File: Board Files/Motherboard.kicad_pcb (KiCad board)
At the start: 2 copper layers, 0 parts

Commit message: + Started board outline + Finished up the schematic (hopefully) + Started creation of custom footprints
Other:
- board outline added: 106 x 155 mm
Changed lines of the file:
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@@
   (general
     (thickness 1.6)
-    (drawings 0)
+    (drawings 5)
     (tracks 0)
     (zones 0)
@@
     (nets 1)
   )
-  (page A4)
+  (page A)
   (layers
     (0 F.Cu signal)
@@
     (uvia_drill 0.1)
   )
+  (gr_line (start 132.87 184.79) (end 34.15 184.79) (layer Edge.Cuts) (width 0.05))
+  (gr_line (start 140.2 177.76) (end 140.2 29.79) (layer Edge.Cuts) (width 0.05))
+  (gr_line (start 140.2 177.76) (end 132.87 184.79) (layer Edge.Cuts) (width 0.05))
+  (gr_line (start 34.15 29.79) (end 140.2 29.79) (layer Edge.Cuts) (width 0.05))
+  (gr_line (start 34.15 29.79) (end 34.15 184.79) (layer Edge.Cuts) (width 0.05))
 )

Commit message: + Completed schematic + Added RF Modulator schematic symbol + Added RF Modulator footprint + Added Reset Switch footprint + Completed Power Switch footprint + Continued board layout
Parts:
- added ACPLUG1: , Connector_BarrelJack:BarrelJack_CUI_PJ-102AH_Horizontal, F.Cu at (48.4, 6.95)
- added BC1: 10nF, Capacitor_THT:C_Disc_D6.0mm_W2.5mm_P5.00mm, F.Cu at (-118.4, -29.9)
- added C1: 100uF, Capacitor_THT:CP_Radial_D5.0mm_P2.50mm, F.Cu at (-85.6, -45.9)
- added C10: 10nF, Capacitor_THT:C_Disc_D3.0mm_W1.6mm_P2.50mm, F.Cu at (-125.3, -30.3)
- added C11: 0.47uF, Capacitor_THT:CP_Radial_D5.0mm_P2.50mm, F.Cu at (-85.6, -39.3)
- added C12: 10nF, Capacitor_THT:C_Disc_D3.0mm_W1.6mm_P2.50mm, F.Cu at (-118.4, -26.3)
- added C13: 1500uF, Capacitor_THT:CP_Radial_D12.5mm_P5.00mm, F.Cu at (87.5, -10.7)
- added C14: 1uF, Capacitor_THT:CP_Radial_D5.0mm_P2.50mm, F.Cu at (-79.0, -45.9)
- added C14: 1uF, Capacitor_THT:CP_Radial_D5.0mm_P2.50mm, F.Cu at (81.6, -15.8)
- added C15: 330pF, Capacitor_THT:C_Disc_D3.0mm_W1.6mm_P2.50mm, F.Cu at (-109.4, -18.2)
- added C16: 330pF, Capacitor_THT:C_Disc_D3.0mm_W1.6mm_P2.50mm, F.Cu at (-90.8, -34.5)
- added C17: 330pF, Capacitor_THT:C_Disc_D3.0mm_W1.6mm_P2.50mm, F.Cu at (-95.5, -29.9)
- added C19: 330pF, Capacitor_THT:C_Disc_D3.0mm_W1.6mm_P2.50mm, F.Cu at (-79.5, -41.0)
- added C2: 330pF, Capacitor_THT:C_Disc_D3.0mm_W2.0mm_P2.50mm, F.Cu at (-89.8, -31.1)
- added C20: 330pF, Capacitor_THT:C_Disc_D3.0mm_W1.6mm_P2.50mm, F.Cu at (-95.5, -26.7)
- added C21: 330pF, Capacitor_THT:C_Disc_D3.0mm_W1.6mm_P2.50mm, F.Cu at (-103.7, -19.8)
- added C22: 330pF, Capacitor_THT:C_Disc_D3.0mm_W1.6mm_P2.50mm, F.Cu at (-98.8, -23.3)
- added C23: 330pF, Capacitor_THT:C_Disc_D3.0mm_W1.6mm_P2.50mm, F.Cu at (-85.2, -34.5)
- added C24: 10nF, Capacitor_THT:C_Disc_D5.0mm_W2.5mm_P5.00mm, F.Cu at (-94.3, -47.2)
- added C25: 330pF, Capacitor_THT:C_Disc_D3.0mm_W1.6mm_P2.50mm, F.Cu at (-79.5, -37.9)
- added C26: 330pF, Capacitor_THT:C_Disc_D3.0mm_W1.6mm_P2.50mm, F.Cu at (-89.8, -27.8)
- added C27: 10nF, Capacitor_THT:C_Disc_D5.0mm_W2.5mm_P5.00mm, F.Cu at (-99.0, -37.5)
- added C28: 10nF, Capacitor_THT:C_Disc_D6.0mm_W2.5mm_P5.00mm, F.Cu at (-99.0, -33.5)
- added C3: 1uF, Capacitor_THT:CP_Radial_D5.0mm_P2.50mm, F.Cu at (-101.6, -28.2)
- added C30: 10nF, Capacitor_THT:C_Disc_D5.0mm_W2.5mm_P5.00mm, F.Cu at (-112.6, -25.8)
- added C31: 10nF, Capacitor_THT:C_Disc_D5.0mm_W2.5mm_P5.00mm, F.Cu at (-91.8, -51.6)
- added C36: 10nF, Capacitor_THT:C_Disc_D5.0mm_W2.5mm_P5.00mm, F.Cu at (-112.6, -21.8)
- added C37: 10nF, Capacitor_THT:C_Disc_D5.0mm_W2.5mm_P5.00mm, F.Cu at (-94.3, -43.2)
- added C38: 10nF, Capacitor_THT:C_Disc_D5.0mm_W2.5mm_P5.00mm, F.Cu at (-83.7, -51.2)
- added C46: 100nF, Capacitor_THT:C_Disc_D7.0mm_W2.5mm_P5.00mm, F.Cu at (-131.5, -17.9)
- added C5: 10nF, Capacitor_THT:C_Disc_D5.0mm_W2.5mm_P5.00mm, F.Cu at (-110.3, -30.7)
- added C6: 10nF, Capacitor_THT:C_Disc_D5.0mm_W2.5mm_P5.00mm, F.Cu at (-123.2, -17.9)
- added C7: 330pF, Capacitor_THT:C_Disc_D3.0mm_W1.6mm_P2.50mm, F.Cu at (-98.1, -20.2)
- added C8: 10nF, Capacitor_THT:C_Disc_D3.0mm_W2.0mm_P2.50mm, F.Cu at (-115.0, -18.0)
- added C9: 10pF, Capacitor_THT:C_Disc_D3.0mm_W2.0mm_P2.50mm, F.Cu at (-104.5, -23.1)
- added DA1: DAN601, Resistor_THT:R_Array_SIP7, F.Cu at (34.7, -127.1)
- added DA2: UPA64H, Resistor_THT:R_Array_SIP7, F.Cu at (34.7, -124.5)
- added DA3: DAN601, Resistor_THT:R_Array_SIP7, F.Cu at (14.5, -127.1)
- added DA4: UPA64H, Resistor_THT:R_Array_SIP7, F.Cu at (14.5, -124.5)
- added DB1: RC203, Diode_THT:Diode_Bridge_Round_D9.0mm, F.Cu at (75.8, -15.2)
- added FC1: 39u, Resistor_THT:R_Axial_DIN0207_L6.3mm_D2.5mm_P10.16mm_Horizontal, F.Cu at (-112.3, -34.8)
- added FC2: Ferrite_Coil, Resistor_THT:R_Axial_DIN0207_L6.3mm_D2.5mm_P10.16mm_Horizontal, F.Cu at (-145.0, -26.7)
- added P1: 72-Pin Connector, Toploader:Cart Connector, F.Cu at (9.25, -32.2)
- added P2: PowerSw, Toploader:PowerSwitch, F.Cu at (96.8, -122.5)
- added P3: ResetSw, Toploader:ResetSwitch, F.Cu at (75.6, -127.3)
- added P4: Controller_Port, Toploader:Controller Ports, F.Cu at (10.8, -137.5)
- added Q1: 2SA937, Package_TO_SOT_THT:TO-126-3_Vertical, F.Cu at (-121.5, -21.9)
- added Q2: 2SC2021, Package_TO_SOT_THT:TO-126-3_Vertical, F.Cu at (-131.1, -21.9)
- added R10: 150, Resistor_THT:R_Axial_DIN0207_L6.3mm_D2.5mm_P10.16mm_Horizontal, F.Cu at (-145.0, -22.7)
- added R2: 430, Resistor_THT:R_Axial_DIN0207_L6.3mm_D2.5mm_P10.16mm_Horizontal, F.Cu at (-112.3, -38.8)
- added R4: 160, Resistor_THT:R_Axial_DIN0207_L6.3mm_D2.5mm_P10.16mm_Horizontal, F.Cu at (-105.1, -51.3)
- added R5: 160, Resistor_THT:R_Axial_DIN0207_L6.3mm_D2.5mm_P10.16mm_Horizontal, F.Cu at (-112.3, -42.9)
- added R6: 200, Resistor_THT:R_Axial_DIN0207_L6.3mm_D2.5mm_P10.16mm_Horizontal, F.Cu at (-112.3, -46.9)
- added R7: 100, Resistor_THT:R_Axial_DIN0207_L6.3mm_D2.5mm_P10.16mm_Horizontal, F.Cu at (-145.0, -18.6)
- added R8: 150K, Resistor_THT:R_Axial_DIN0207_L6.3mm_D2.5mm_P10.16mm_Horizontal, F.Cu at (-131.7, -26.7)
- added R9: 1.2K, Resistor_THT:R_Axial_DIN0207_L6.3mm_D2.5mm_P10.16mm_Horizontal, F.Cu at (-92.9, -55.6)
- added RA1: 12 x 10K, Resistor_THT:R_Array_SIP12, F.Cu at (14.5, -122.0)
- added REF**: RF-MOD, Toploader:RF-MOD, F.Cu at (37.5, -19.2)
- added TC1: 30pF, Toploader:TrimmerCap-THT, F.Cu at (-79.5, -56.9)
- added U1: 6116 (WRAM), Package_DIP:DIP-24_W7.62mm, F.Cu at (17.0, -45.5)
- added U2: 74HC373, Package_DIP:DIP-20_W7.62mm, F.Cu at (57.5, -57.5)
- added U3: 74HC139, Package_DIP:DIP-16_W7.62mm, F.Cu at (24.5, -57.5)
- added U4: 6116 (VRAM), Package_DIP:DIP-24_W7.62mm, F.Cu at (57.8, -45.5)
- added U5: RP2C02 PPU, Package_DIP:DIP-40_W15.24mm, F.Cu at (14.6, -90.0)
- added U6: RP2A03 CPU, Package_DIP:DIP-40_W15.24mm, F.Cu at (37.5, -69.5)
- added U7: 40H368 (CI), Package_DIP:DIP-16_W7.62mm, F.Cu at (47.2, -110.8)
- added U8: 40H368 (CII), Package_DIP:DIP-16_W7.62mm, F.Cu at (21.0, -110.8)
- added U9: L7805, Connector_PinHeader_2.54mm:PinHeader_1x03_P2.54mm_Vertical, F.Cu at (51.8, -16.2)
- added X1: 21.47727 MHz, Crystal:Crystal_HC49-U_Vertical, F.Cu at (81.2, -112.0)
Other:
- board size 106 x 155 mm -> 106.1 x 155 mm

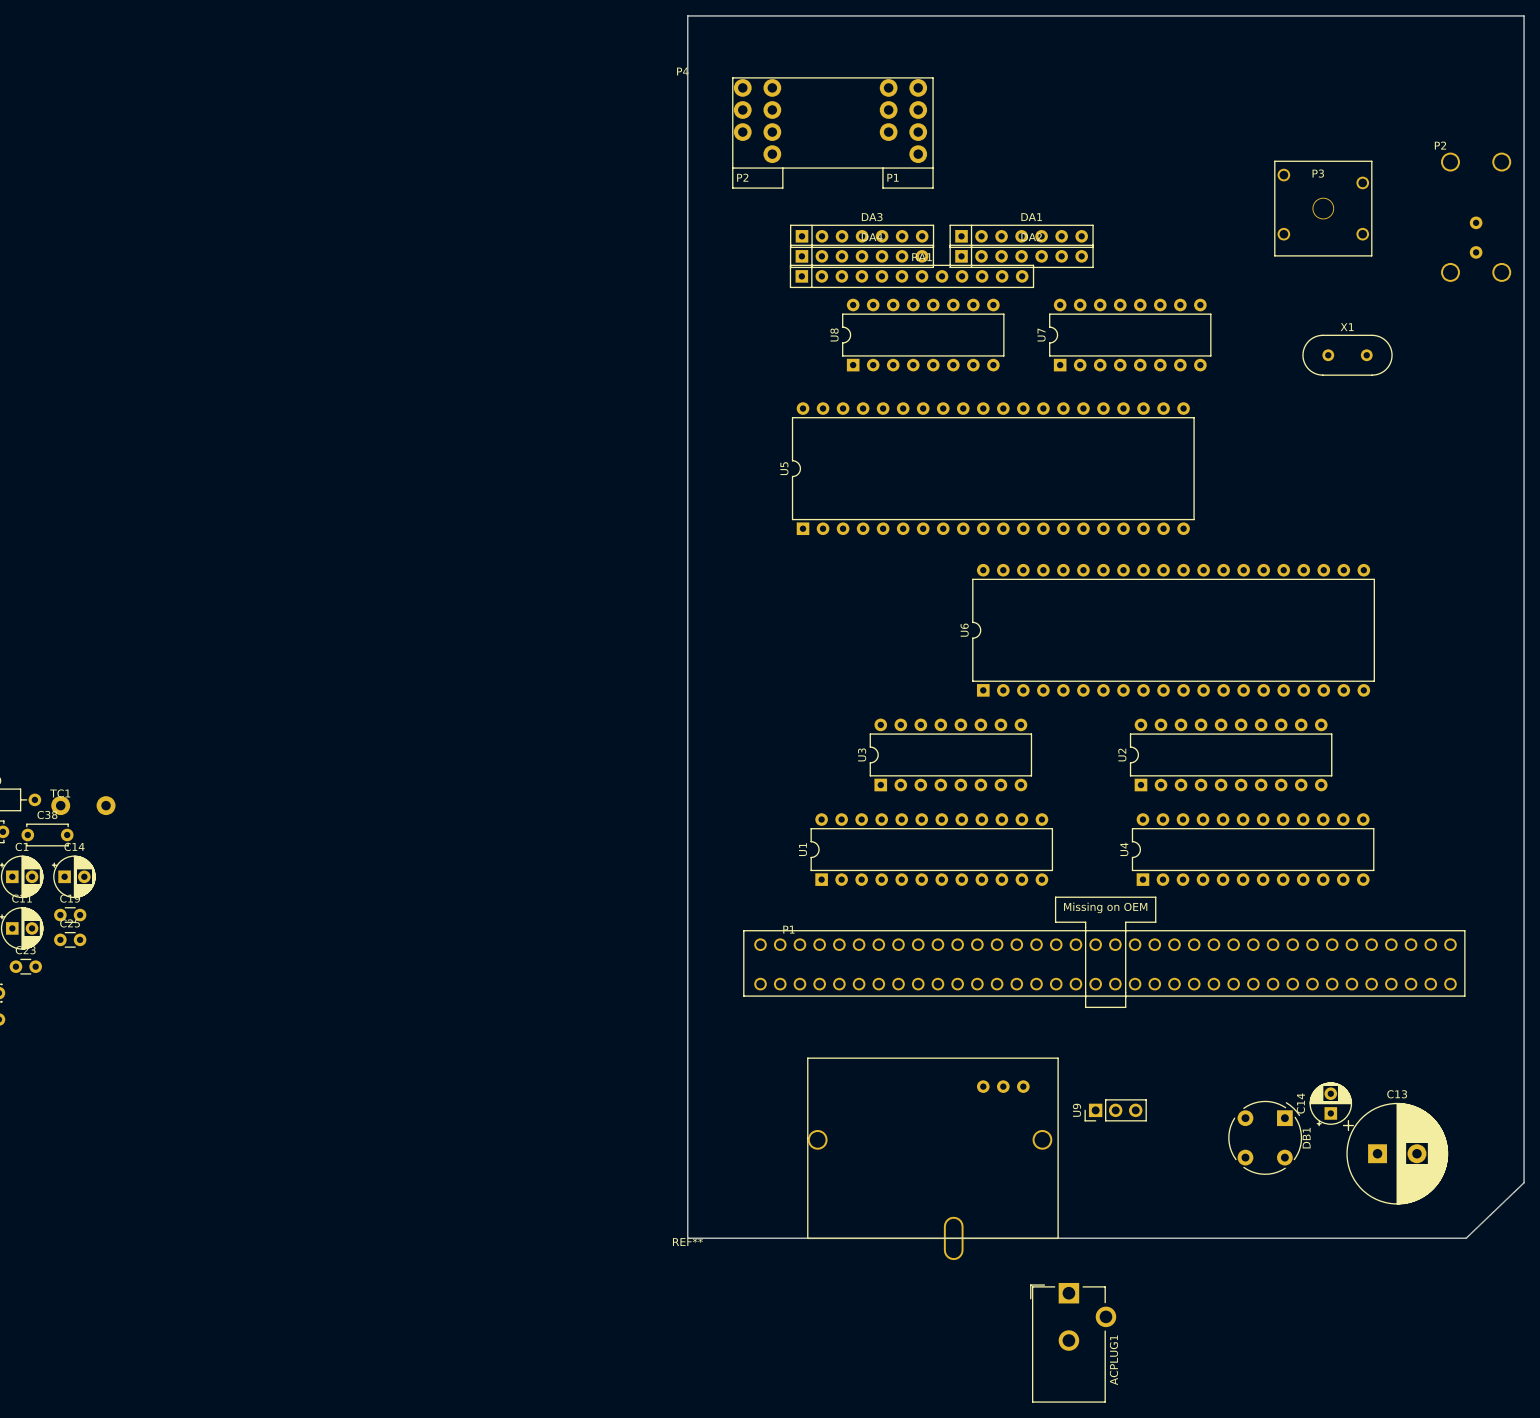
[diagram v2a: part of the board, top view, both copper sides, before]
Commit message: + Added screw holes to PCB + Added holes to Cartridge and Controller footprints
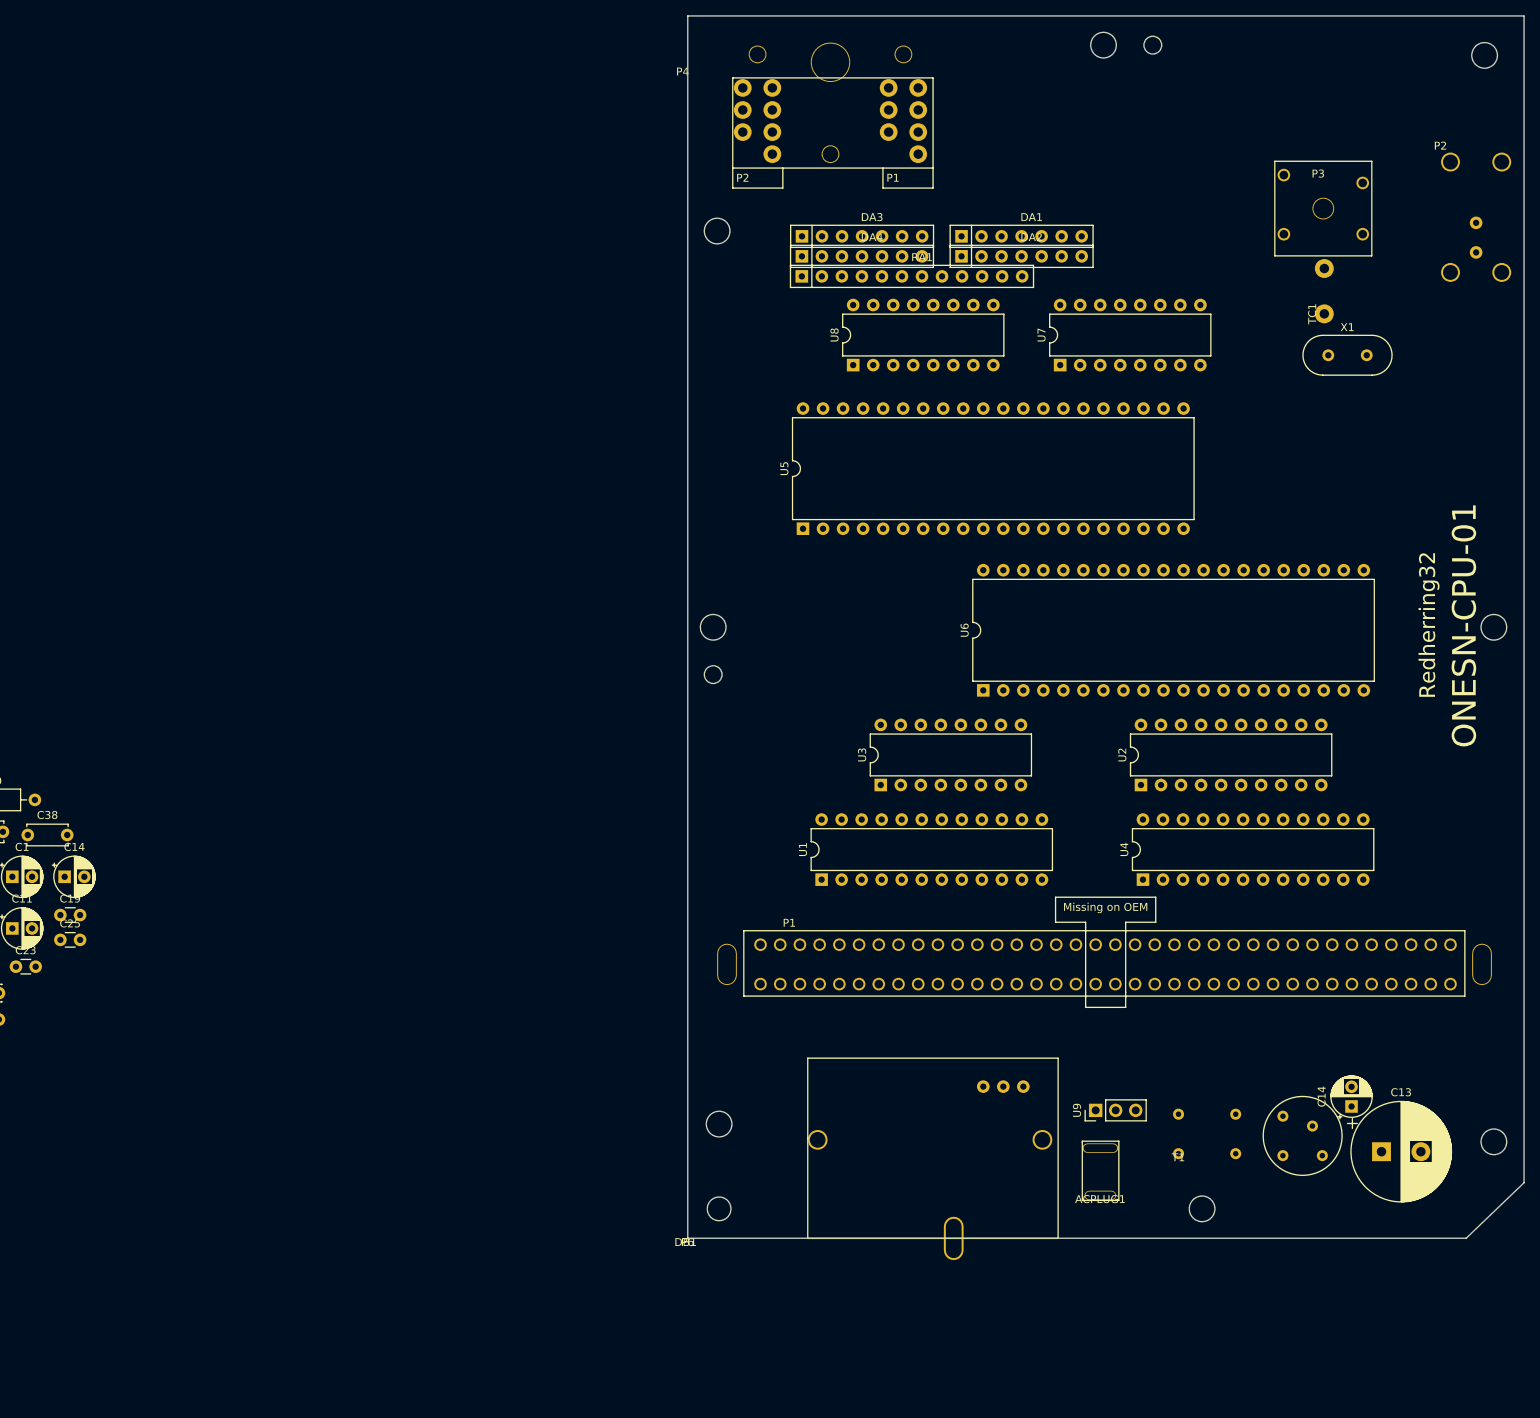
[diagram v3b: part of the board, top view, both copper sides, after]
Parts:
- removed REF**: RF-MOD, Toploader:RF-MOD
- added P6: RF-Mod, Toploader:RF-MOD, F.Cu at (37.5, -19.2)
- added T1: 08RB01, Toploader:Inductor, F.Cu at (62.2, -10.8)
- ACPLUG1: footprint Connector_BarrelJack:BarrelJack_CUI_PJ-102AH_Horizontal -> Toploader:AC-JACK
- DB1: footprint Diode_THT:Diode_Bridge_Round_D9.0mm -> Toploader:Rectifier
- moved TC1 171.2 mm to (80.8, -117.2), turned to 90 degrees
- moved ACPLUG1 13.0 mm to (52.4, -5.45)
- moved DB1 4.76 mm to (75.5, -10.5), turned to 0 degrees
- moved C14 2.77 mm to (84.2, -16.7)
- moved C13 0.56 mm to (88.0, -11.0)
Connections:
- C13 pad 2: Net-(C13-Pad2) -> /GND
- C14 pad 2: Net-(C13-Pad2) -> /GND
- DB1 pad 2: Net-(C13-Pad2) -> /GND
- P2 pad 3: Net-(C13-Pad2) -> /GND
- U9 pad 2: Net-(C13-Pad2) -> /GND
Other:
- outline, holes or cut-outs redrawn
- board text added: "ONESN-CPU-01"
- board text added: "Redherring32"

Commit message: + Finished component layout + Tidied silkscreen
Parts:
- removed the C14 at (-79.0, -45.9)
- removed C46: 100nF, Capacitor_THT:C_Disc_D7.0mm_W2.5mm_P5.00mm
- added C18: 10nF, Capacitor_THT:C_Disc_D3.0mm_W1.6mm_P2.50mm, F.Cu at (42.2, -134.5)
- added C29: 10nF, Capacitor_THT:C_Disc_D3.0mm_W2.0mm_P2.50mm, F.Cu at (17.2, -65.0)
- added C32: 10nF, Capacitor_THT:C_Disc_D3.0mm_W2.0mm_P2.50mm, F.Cu at (86.8, -59.8)
- added C33: 10nF, Capacitor_THT:C_Disc_D3.0mm_W2.0mm_P2.50mm, F.Cu at (29.2, -81.8)
- added C34: 10nF, Capacitor_THT:C_Disc_D3.0mm_W2.0mm_P2.50mm, F.Cu at (90.8, -72.5)
- added C35: 10nF, Capacitor_THT:C_Disc_D3.0mm_W2.0mm_P2.50mm, F.Cu at (71.0, -94.8)
- added C4: 220pF, Capacitor_THT:C_Disc_D3.0mm_W1.6mm_P2.50mm, F.Cu at (14.8, -79.0)
- added R1: 510, Resistor_THT:R_Axial_DIN0207_L6.3mm_D2.5mm_P10.16mm_Horizontal, F.Cu at (75.5, -91.8)
- added R3: 150, Resistor_THT:R_Axial_DIN0207_L6.3mm_D2.5mm_P10.16mm_Horizontal, F.Cu at (90.8, -58.0)
- C24: footprint Capacitor_THT:C_Disc_D5.0mm_W2.5mm_P5.00mm -> Capacitor_THT:C_Disc_D3.0mm_W1.6mm_P2.50mm
- C27, C30, C31, C36, C37, C38, C5, C6: footprint Capacitor_THT:C_Disc_D5.0mm_W2.5mm_P5.00mm -> Capacitor_THT:C_Disc_D3.0mm_W2.0mm_P2.50mm
- C28: footprint Capacitor_THT:C_Disc_D6.0mm_W2.5mm_P5.00mm -> Capacitor_THT:C_Disc_D3.0mm_W2.0mm_P2.50mm
- moved R10 238.1 mm to (78.8, -104.0)
- moved Q2 224.3 mm to (76.0, -108.2), turned to 90 degrees
- moved Q1 224.3 mm to (90.8, -94.5), turned to 90 degrees
- moved R8 220.9 mm to (72.5, -110.8), turned to 90 degrees
- moved C9 212.6 mm to (86.4, -116.8), turned to 90 degrees
- moved C8 210.8 mm to (78.8, -101.0)
- moved C10 210.6 mm to (69.2, -110.8), turned to 90 degrees
- moved R2 207.1 mm to (90.8, -79.5), turned to 90 degrees
- moved C7 198.9 mm to (75.8, -116.8), turned to 90 degrees
- moved BC1 195.9 mm to (45.2, -137.5), turned to 270 degrees
- moved FC2 192.8 mm to (47.8, -24.2)
- moved C31 184.8 mm to (93.0, -54.5), turned to 180 degrees
- moved C11 184.3 mm to (69.2, -139.2), turned to 90 degrees
- moved C15 184.1 mm to (33.2, -134.5), turned to 270 degrees
- moved C20 182.1 mm to (51.2, -134.5), turned to 270 degrees
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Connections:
- C10 pad 1: Net-(C10-Pad1) -> /SYS-CLK
- C10 pad 2: /SYS-CLK -> Net-(C10-Pad2)
- C2 pad 1: /VIDEO -> /GND
- C2 pad 2: /GND -> /VIDEO
- C24 pad 2: /VCC -> Net-(C24-Pad2)
- C5 pad 1: /GND -> /AUDIO
- C5 pad 2: /AUDIO -> /GND
- C8 pad 1: /GND -> Net-(C8-Pad1)
- C8 pad 2: Net-(C8-Pad2) -> /GND
- FC1 pad 1: (no net) -> /AUDIO
- FC1 pad 2: (no net) -> Net-(C3-Pad1)
- FC2 pad 1: Net-(FC2-Pad1) -> /VIDEO
- FC2 pad 2: /VIDEO -> Net-(FC2-Pad2)
- Q2 pad 1: Net-(C8-Pad2) -> Net-(C8-Pad1)
- Q2 pad 2: Net-(C10-Pad1) -> Net-(C10-Pad2)
- R10 pad 1: Net-(C8-Pad2) -> Net-(C8-Pad1)
- R2 pad 1: Net-(FC2-Pad1) -> Net-(FC2-Pad2)
- R8 pad 1: Net-(C10-Pad1) -> Net-(C10-Pad2)
- R9 pad 2: Net-(C10-Pad1) -> Net-(C10-Pad2)
- X1 pad 1: Net-(C10-Pad1) -> Net-(C10-Pad2)
